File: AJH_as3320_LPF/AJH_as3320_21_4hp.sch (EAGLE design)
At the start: 58 parts, among them IC1 TL072D, IC2 CEM3320QFN24, IC3 LM4040 5.0V, IC4 TL074D, J1 PJ301_THONKICONN6, J2 PJ301_THONKICONN6, J3 PJ301_THONKICONN6, J4 PJ301_THONKICONN6

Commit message: Maded Multisheet and added input buffer
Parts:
- IC1: value TL072D -> TL074D; device linear:TL072D -> linear:TL074D
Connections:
- new net N$9: IC1C.+IN, J2.3
- net -12V: no longer IC1P.V-, IC4P.V-
- net 12V: no longer IC1P.V+, IC4P.V+
- net LOWPASS_IN: now also IC1C.-IN, IC1C.OUT; no longer J2.3

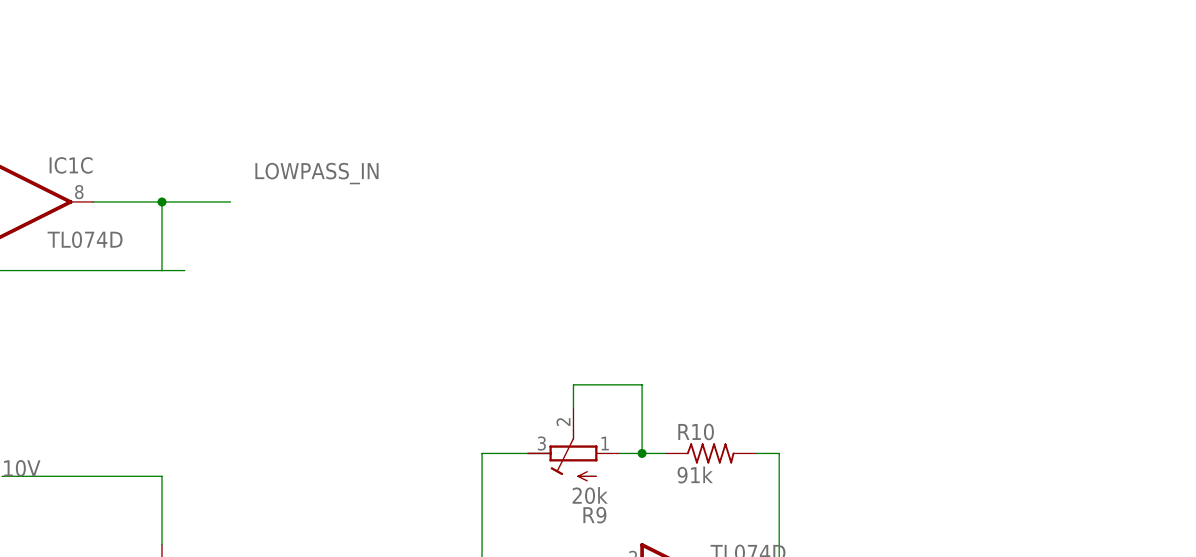
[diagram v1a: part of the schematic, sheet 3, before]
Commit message: Updated power to op-amps
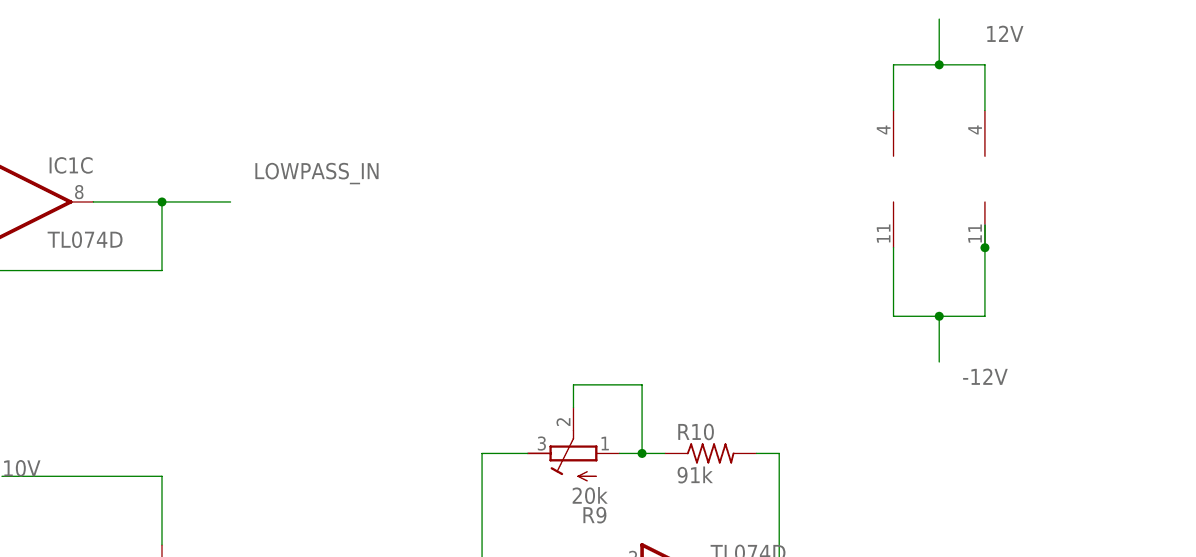
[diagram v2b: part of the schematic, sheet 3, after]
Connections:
- net -12V: now also IC1P.V-, IC4P.V-
- net 12V: now also IC1P.V+, IC4P.V+
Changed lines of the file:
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@@
 <wire x1="-58.42" y1="81.28" x2="-58.42" y2="83.82" width="0.1524" layer="91"/>
 <wire x1="-58.42" y1="83.82" x2="-50.8" y2="83.82" width="0.1524" layer="91"/>
-<wire x1="-43.18" y1="83.82" x2="-50.8" y2="83.82" width="0.1524" layer="91"/>
-<wire x1="-43.18" y1="78.74" x2="-43.18" y2="83.82" width="0.1524" layer="91"/>
-<wire x1="-38.1" y1="83.82" x2="-43.18" y2="83.82" width="0.1524" layer="91"/>
 <wire x1="-66.04" y1="81.28" x2="-66.04" y2="83.82" width="0.1524" layer="91"/>
 <wire x1="-66.04" y1="83.82" x2="-58.42" y2="83.82" width="0.1524" layer="91"/>
-<junction x="-50.8" y="83.82"/>
-<junction x="-43.18" y="83.82"/>
 <junction x="-58.42" y="83.82"/>
 <junction x="-66.04" y="83.82"/>
@@
 <wire x1="-50.8" y1="83.82" x2="-50.8" y2="88.9" width="0.1524" layer="91"/>
 <label x="-50.8" y="88.9" size="1.778" layer="95"/>
-<wire x1="-38.1" y1="83.82" x2="-38.1" y2="78.74" width="0.1524" layer="91"/>
 <pinref part="C1" gate="G$1" pin="1"/>
 <pinref part="C13" gate="G$1" pin="+"/>
@@
 <wire x1="-58.42" y1="60.96" x2="-58.42" y2="58.42" width="0.1524" layer="91"/>
 <wire x1="-58.42" y1="58.42" x2="-50.8" y2="58.42" width="0.1524" layer="91"/>
-<wire x1="-50.8" y1="58.42" x2="-43.18" y2="58.42" width="0.1524" layer="91"/>
-<wire x1="-43.18" y1="63.5" x2="-43.18" y2="58.42" width="0.1524" layer="91"/>
-<wire x1="-43.18" y1="58.42" x2="-38.1" y2="58.42" width="0.1524" layer="91"/>
 <wire x1="-66.04" y1="60.96" x2="-66.04" y2="58.42" width="0.1524" layer="91"/>
 <wire x1="-66.04" y1="58.42" x2="-58.42" y2="58.42" width="0.1524" layer="91"/>
-<junction x="-50.8" y="58.42"/>
-<junction x="-43.18" y="58.42"/>
 <junction x="-58.42" y="58.42"/>
 <junction x="-66.04" y="58.42"/>
@@
 <wire x1="-50.8" y1="58.42" x2="-50.8" y2="50.8" width="0.1524" layer="91"/>
 <label x="-50.8" y="50.8" size="1.778" layer="95"/>
-<wire x1="-38.1" y1="63.5" x2="-38.1" y2="58.42" width="0.1524" layer="91"/>
 <pinref part="C2" gate="G$1" pin="2"/>
 <pinref part="C14" gate="G$1" pin="-"/>
@@
 <attribute name="VALUE" x="68.58" y="111.76" size="1.778" layer="96"/>
 </instance>
+<instance part="IC1" gate="P" x="162.56" y="119.38" smashed="yes"/>
+<instance part="IC4" gate="P" x="172.72" y="119.38" smashed="yes"/>
 </instances>
 <busses>
@@
 <pinref part="IC1" gate="C" pin="OUT"/>
 <wire x1="73.66" y1="116.84" x2="81.28" y2="116.84" width="0.1524" layer="91"/>
+<wire x1="81.28" y1="116.84" x2="88.9" y2="116.84" width="0.1524" layer="91"/>
+<wire x1="81.28" y1="109.22" x2="81.28" y2="116.84" width="0.1524" layer="91"/>
+<junction x="81.28" y="116.84"/>
+<label x="91.44" y="119.38" size="1.778" layer="95"/>
 <pinref part="IC1" gate="C" pin="-IN"/>
-<wire x1="81.28" y1="116.84" x2="88.9" y2="116.84" width="0.1524" layer="91"/>
 <wire x1="58.42" y1="114.3" x2="55.88" y2="114.3" width="0.1524" layer="91"/>
 <wire x1="55.88" y1="114.3" x2="55.88" y2="109.22" width="0.1524" layer="91"/>
 <wire x1="55.88" y1="109.22" x2="81.28" y2="109.22" width="0.1524" layer="91"/>
-<wire x1="83.82" y1="109.22" x2="81.28" y2="109.22" width="0.1524" layer="91"/>
-<wire x1="81.28" y1="109.22" x2="81.28" y2="116.84" width="0.1524" layer="91"/>
-<junction x="81.28" y="116.84"/>
-<label x="91.44" y="119.38" size="1.778" layer="95"/>
-</segment>
-</net>
+</segment>
+</net>
+<net name="12V" class="1">
+<segment>
+<pinref part="IC1" gate="P" pin="V+"/>
+<wire x1="162.56" y1="127" x2="162.56" y2="132.08" width="0.1524" layer="91"/>
+<wire x1="162.56" y1="132.08" x2="167.64" y2="132.08" width="0.1524" layer="91"/>
+<wire x1="167.64" y1="132.08" x2="172.72" y2="132.08" width="0.1524" layer="91"/>
+<wire x1="172.72" y1="132.08" x2="172.72" y2="127" width="0.1524" layer="91"/>
+<pinref part="IC4" gate="P" pin="V+"/>
+<wire x1="167.64" y1="132.08" x2="167.64" y2="137.16" width="0.1524" layer="91"/>
+<junction x="167.64" y="132.08"/>
+<label x="172.72" y="134.62" size="1.778" layer="95"/>
+</segment>
+</net>
+<net name="-12V" class="1">
+<segment>
+<pinref part="IC1" gate="P" pin="V-"/>
+<wire x1="162.56" y1="111.76" x2="162.56" y2="104.14" width="0.1524" layer="91"/>
+<wire x1="162.56" y1="104.14" x2="167.64" y2="104.14" width="0.1524" layer="91"/>
+<wire x1="167.64" y1="104.14" x2="172.72" y2="104.14" width="0.1524" layer="91"/>
+<wire x1="172.72" y1="104.14" x2="172.72" y2="111.76" width="0.1524" layer="91"/>
+<pinref part="IC4" gate="P" pin="V-"/>
+<wire x1="172.72" y1="111.76" x2="172.72" y2="114.3" width="0.1524" layer="91"/>
+<junction x="172.72" y="111.76"/>
+<wire x1="167.64" y1="104.14" x2="167.64" y2="99.06" width="0.1524" layer="91"/>
+<junction x="167.64" y="104.14"/>
+<label x="170.18" y="96.52" size="1.778" layer="95"/>
+</segment>
+</net>

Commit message: First Bandpass Circuit
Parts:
- removed C9: 300pF, rcl:C-USC0603
- removed R14, R15: 91k, rcl:R-US_R0603
- removed R16: 220k, rcl:R-US_R0603
- added C15: 300pF, rcl:C-USC0603
- IC2: value CEM3320QFN24 -> CEM3320; device CEM:CEM3320QFN24 -> CEM:CEM3320
- R25: value 49.9k -> 68K
- renumbered J1 to FM_IN, J2 to SIGNALIN, J3 to V-OCT, J4 to OUTPUT
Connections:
- net LOWPASS_OUT renamed BANDPASS_OUT
- removed net LOWPASS_IN: IC1C.-IN, IC1C.OUT, R14.2
- removed net N$41: C8.2, IC2.4
- removed net N$42: C9.2, IC2.5
- removed net N$45: IC2.1, R14.1, R18.1
- removed net N$46: IC2.7, R18.2, R20.2
- removed net N$47: IC2.6, R19.1, R22.2
- removed net N$49: IC2.15, R15.1, R21.1
- removed net N$50: C12.+, IC2.10, R12.1
- removed net N$52: IC2.2, R16.2, R20.1, R22.1
- removed net N$53: IC2.17, R17.1, R19.2, R21.2
- new net BANDPASS_IN: C15.1, IC1C.-IN, IC1C.OUT
- new net N$14: IC2.15, R18.1, R19.1
- new net N$16: IC2.18, R13.1, R19.2, R21.2
- new net N$17: C12.+, IC2.10, R21.1
- new net N$19: C15.2, IC2.5
- new net N$23: C8.2, IC2.7, R12.1
- new net N$24: C8.1, IC2.4
- new net N$25: IC2.2, R22.1
- new net N$26: IC2.6, R20.2, R22.2
- new net N$27: IC2.1, R12.2
- net -12V: no longer R16.1
- net GND: no longer C8.1, C9.1
- net N$2: now also IC2.17, R17.1, R18.2, R20.1; no longer IC2.18, R12.2, R13.1, R15.2
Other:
- note added: "Based on : https://github.com/acobley/Analog-Voice By Forest Caver CC-BY-NC-SA 4.0"
